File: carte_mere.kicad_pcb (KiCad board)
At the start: 4 copper layers, 56 x 142.1 mm, 298 parts, among them J1 Conn_01x02_Pin, J10 Conn_01x02_Pin, J11 Conn_01x02_Pin, J12 Conn_01x02_Pin, J13 Conn_01x02_Pin, J14 Conn_01x02, J15 Conn_01x04, J16 Conn_01x03_Pin, J17 Conn_01x05_Pin, J2 Conn_01x03_Pin, J20 Conn_01x04, J21 Conn_01x04, J22 Conn_01x04, J23 Conn_01x02, J24 Conn_01x02, J25 Conn_01x02_Pin, J26 Conn_01x02_Pin, J27 Conn_01x02_Pin, J28 Conn_01x02_Pin, J29 Conn_01x02_Pin, J3 Conn_01x03_Pin, J30 Conn_01x02_Pin, J31 Conn_01x03_Pin, J32 Conn_01x03_Pin, J33 Conn_01x03_Pin, J34 Conn_01x03_Pin, J35 Conn_01x03_Pin, J36 Conn_01x03_Pin, J37 Conn_01x03_Pin, J38 Conn_01x03_Pin, J39 Conn_01x05_Pin, J4 Conn_01x03_Pin, J40 Conn_01x05_Pin, J5 Conn_01x03_Pin, J6 Conn_01x03_Pin, J7 Conn_01x03_Pin, J8 Conn_01x03_Pin, J9 Conn_01x03_Pin, Q1 MMBT3906, Q10 2N7002, Q11 MMBT3906, Q12 AO3401A, Q13 2N7002, Q14 MMBT3906, Q15 AO3401A, Q16 2N7002, Q17 MMBT3906, Q18 AO3401A, Q19 2N7002, Q2 2N7002, Q20 2N7002, Q21 2N7002, Q22 2N7002, Q23 2N7002, Q24 2N7002, Q25 2N7002, Q26 2N7002, Q27 2N7002, Q28 2N7002, Q29 2N7002, Q3 AO3401A, Q30 2N7002, Q31 2N7002, Q32 2N7002, Q33 2N7002, Q34 2N7002, Q37 2N7002, Q38 2N7002, Q39 2N7002, Q4 2N7002, Q40 2N7002, Q5 MMBT3906, Q6 AO3401A, Q7 2N7002, Q8 MMBT3906, Q9 AO3401A, U1 SN65HVD230, U10 SN74LV1T34DCK, U11 SN74LV1T34DCK, U12 SN74LV1T34DCK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

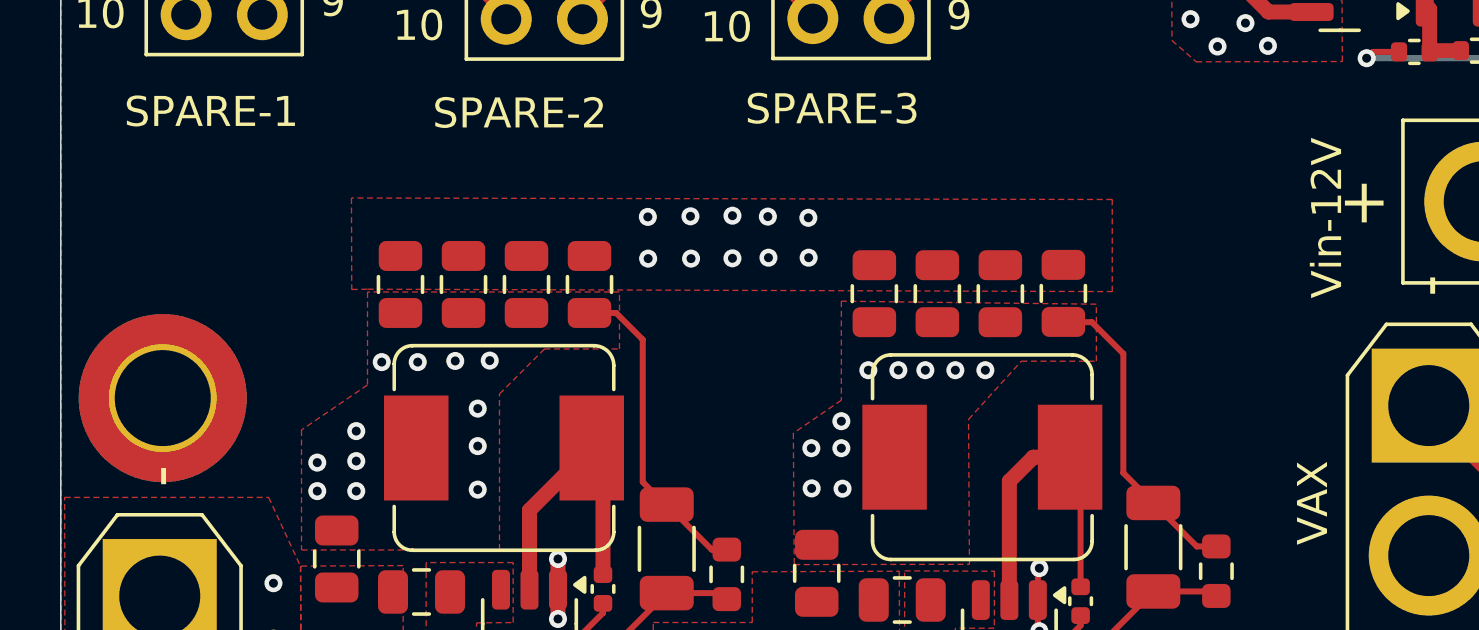
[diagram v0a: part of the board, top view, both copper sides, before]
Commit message: add connectors on alim
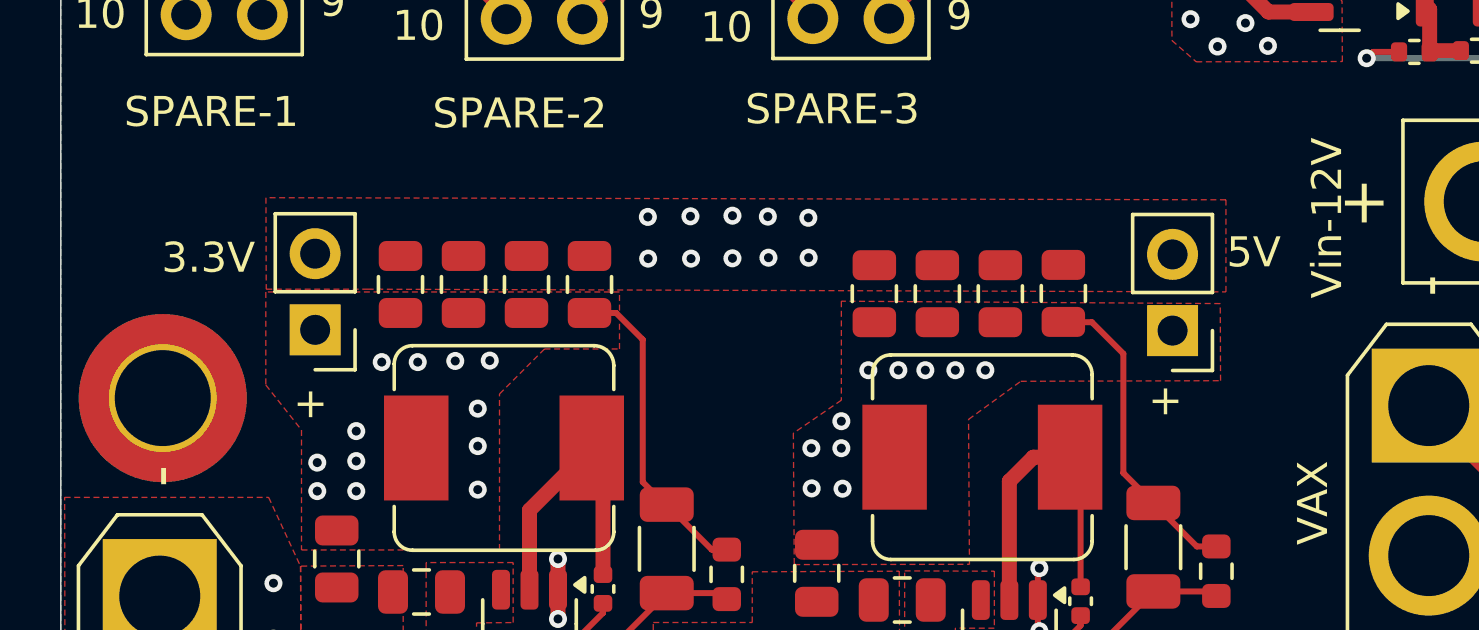
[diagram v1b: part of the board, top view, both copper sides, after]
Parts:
- added J18: Conn_01x02, Connector_PinHeader_2.54mm:PinHeader_1x02_P2.54mm_Vertical, F.Cu at (58.5, 174.7)
- added J19: Conn_01x02, Connector_PinHeader_2.54mm:PinHeader_1x02_P2.54mm_Vertical, F.Cu at (87.1, 174.8)
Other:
- board text added: "+"

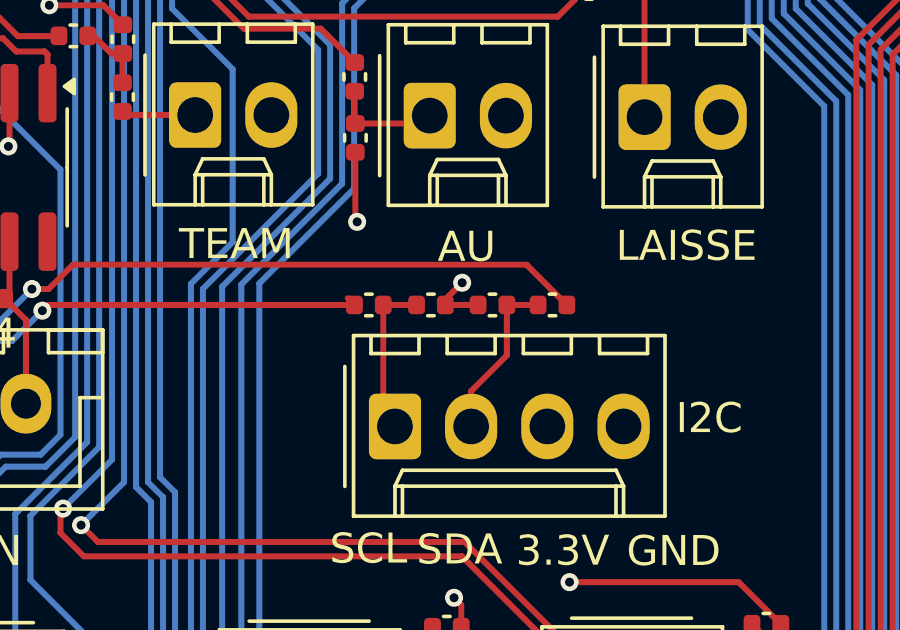
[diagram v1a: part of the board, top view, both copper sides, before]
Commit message: fix issue on i2c
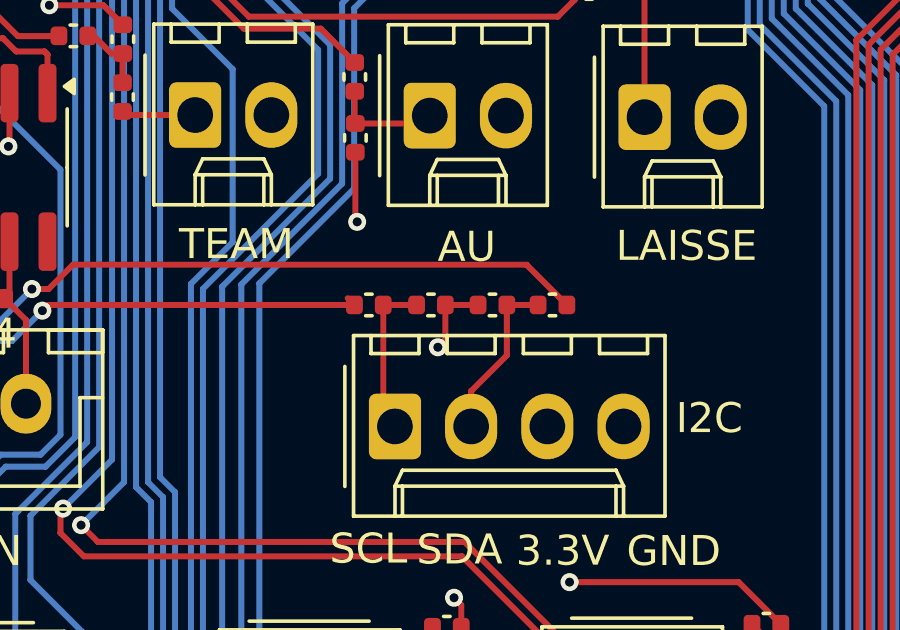
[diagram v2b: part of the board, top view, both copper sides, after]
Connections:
- R118 pad 1: 5V -> 3.3V
- R119 pad 1: 5V -> 3.3V
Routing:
- net 3.3V: track 92.7 -> 95.3 mm, vias 23 -> 24
- net 5V: track 32.4 -> 30.3 mm, vias 16 -> 15
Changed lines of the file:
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@@
 		)
 		(fp_text user "${REFERENCE}"
-			(at 0 1.27 270)
+			(at 0 1.27 -90)
 			(layer "F.Fab")
 			(effects
@@
 			(layers "F.Cu" "F.Paste" "F.Mask")
 			(roundrect_rratio 0.25)
-			(net 58 "5V")
+			(net 15 "3.3V")
 			(pintype "passive")
 		)
@@
 		)
 		(fp_text user "${REFERENCE}"
-			(at 0 1.27 270)
+			(at 0 1.27 -90)
 			(layer "F.Fab")
 			(effects
@@
 			(layers "F.Cu" "F.Paste" "F.Mask")
 			(roundrect_rratio 0.25)
-			(net 58 "5V")
+			(net 15 "3.3V")
 			(pintype "passive")
 		)
@@
 	)
 	(segment
+		(start 69.48 121.71)
+		(end 69.48 122.87)
+		(width 0.2)
+		(layer "F.Cu")
+		(net 15)
+	)
+	(segment
 		(start 73.585 69.93)
 		(end 73.585 69.58)
@@
 	)
 	(segment
+		(start 70.57 121.71)
+		(end 69.48 121.71)
+		(width 0.2)
+		(layer "F.Cu")
+		(net 15)
+	)
+	(segment
 		(start 72.2 182.05)
 		(end 71.7 182.05)
@@
 	)
 	(segment
+		(start 69.48 122.87)
+		(end 69.23 123.12)
+		(width 0.2)
+		(layer "F.Cu")
+		(net 15)
+	)
+	(segment
 		(start 73.69 101.37)
 		(end 73.69 100.2075)
@@
 	)
 	(via
+		(at 69.23 123.12)
+		(size 0.6)
+		(drill 0.3)
+		(layers "F.Cu" "B.Cu")
+		(net 15)
+	)
+	(via
 		(at 58.55 180.1)
 		(size 0.6)
@@
 	)
 	(segment
-		(start 69.48 121.71)
-		(end 69.48 121.53)
-		(width 0.2)
-		(layer "F.Cu")
-		(net 58)
-	)
-	(segment
 		(start 85.42 175.52)
 		(end 84.37 174.47)
@@
 	)
 	(segment
-		(start 69.48 121.53)
-		(end 70.04 120.97)
-		(width 0.2)
-		(layer "F.Cu")
-		(net 58)
-	)
-	(segment
 		(start 68.86 137.57)
 		(end 68.83 137.57)
@@
 	)
 	(segment
-		(start 70.57 121.71)
-		(end 69.48 121.71)
-		(width 0.2)
-		(layer "F.Cu")
-		(net 58)
-	)
-	(segment
 		(start 79.508953 142.72)
 		(end 75.688953 138.9)
@@
 	)
 	(via
-		(at 70.04 120.97)
-		(size 0.6)
-		(drill 0.3)
-		(layers "F.Cu" "B.Cu")
-		(net 58)
-	)
-	(via
 		(at 78.83 136.75)
 		(size 0.6)
@@
 		(polygon
 			(pts
-				(xy 76.38 122.78) (xy 67.65 122.79) (xy 67.65 118.38) (xy 53.57 118.35) (xy 53.57 95.97) (xy 57.6 95.84)
+				(xy 76.37 118.36) (xy 67.64 118.37) (xy 67.65 118.38) (xy 53.57 118.35) (xy 53.57 95.97) (xy 57.6 95.84)
 				(xy 57.61 114.39) (xy 76.39 114.25)
 			)
@@
 		(polygon
 			(pts
-				(xy 50.29 118.67) (xy 50.21 50.17) (xy 63.1 50.25) (xy 62.85 95.54) (xy 53.25 95.42) (xy 53.26 118.69)
+				(xy 50.15 119.15) (xy 50.21 50.17) (xy 63.1 50.25) (xy 62.85 95.54) (xy 53.25 95.42) (xy 53.12 119.17)
 			)
 		)
@@
 		(polygon
 			(pts
-				(xy 50.14 146.09) (xy 62.54 146.09) (xy 62.56 135.59) (xy 66.03 131.95) (xy 67.27 132.02) (xy 67.23 118.71)
-				(xy 50.28 118.67)
+				(xy 50.12 146.41) (xy 62.52 146.41) (xy 62.94 134.62) (xy 66.04 131.98) (xy 76.35 129.04) (xy 76.19 118.81)
+				(xy 50.2 118.9)
 			)
 		)

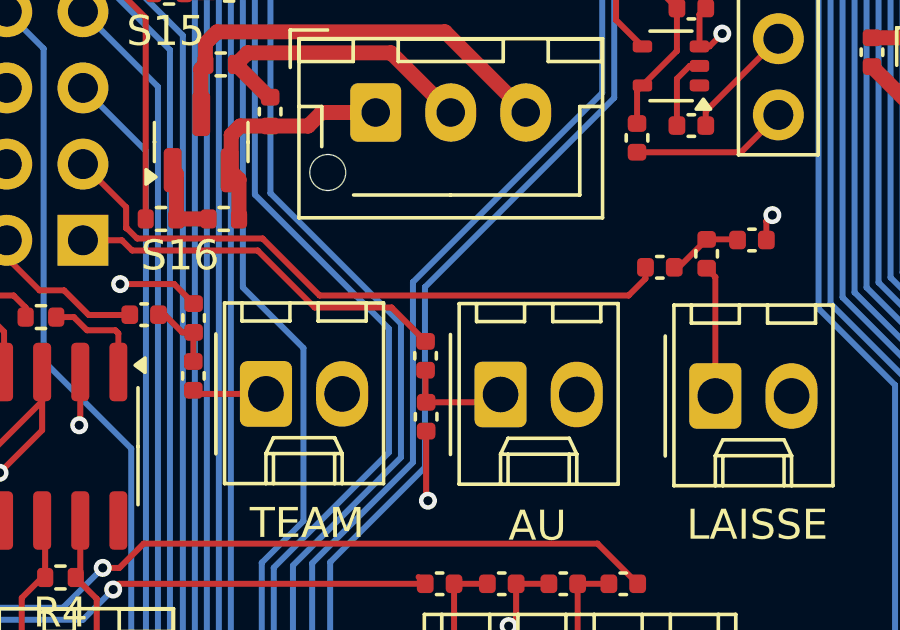
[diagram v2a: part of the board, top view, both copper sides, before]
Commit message: fix switch issue
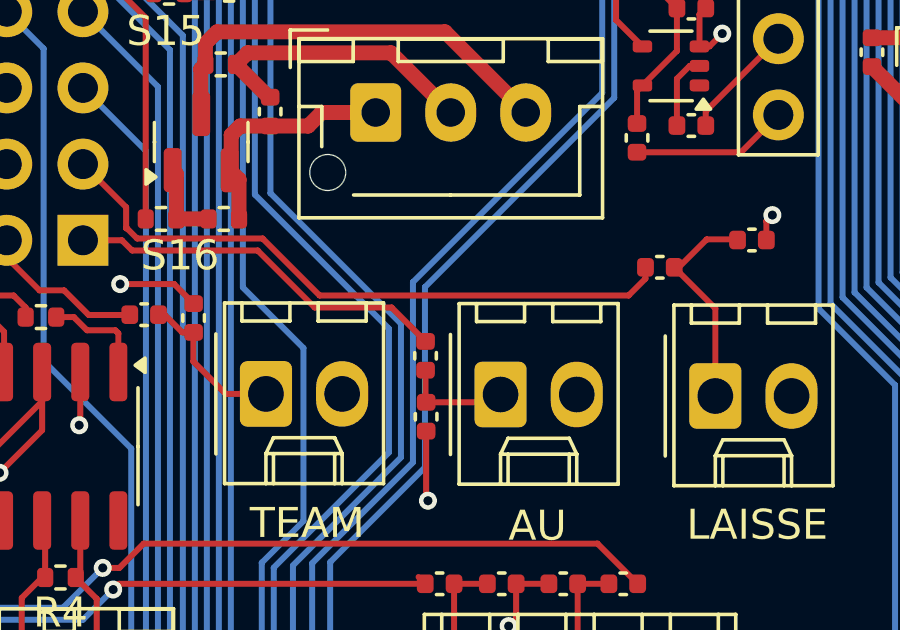
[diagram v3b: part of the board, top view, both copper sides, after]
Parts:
- removed R125, R152: 2k, Capacitor_SMD:C_0402_1005Metric
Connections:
- R116 pad 2: Net-(R116-Pad2) -> Net-(J14-Pin_1)
- R120 pad 2: Net-(R116-Pad2) -> Net-(J14-Pin_1)
- R150 pad 2: Net-(R125-Pad1) -> Net-(J24-Pin_1)
- R151 pad 2: Net-(R125-Pad1) -> Net-(J24-Pin_1)
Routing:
- net Net-(J14-Pin_1): track 4.38 -> 7.39 mm
- net Net-(J24-Pin_1): track 3.26 -> 6.08 mm
- net Net-(R116-Pad2): track 2.53 -> 0.00 mm
- net Net-(R125-Pad1): track 2.39 -> 0.00 mm
